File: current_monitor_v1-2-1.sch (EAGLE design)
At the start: 44 parts, among them IC1 LM4558D, SW1 RESET, SW2 Display, SW3 Display, U1 ATMEGA32U4-XUAU, Y1 16MHz

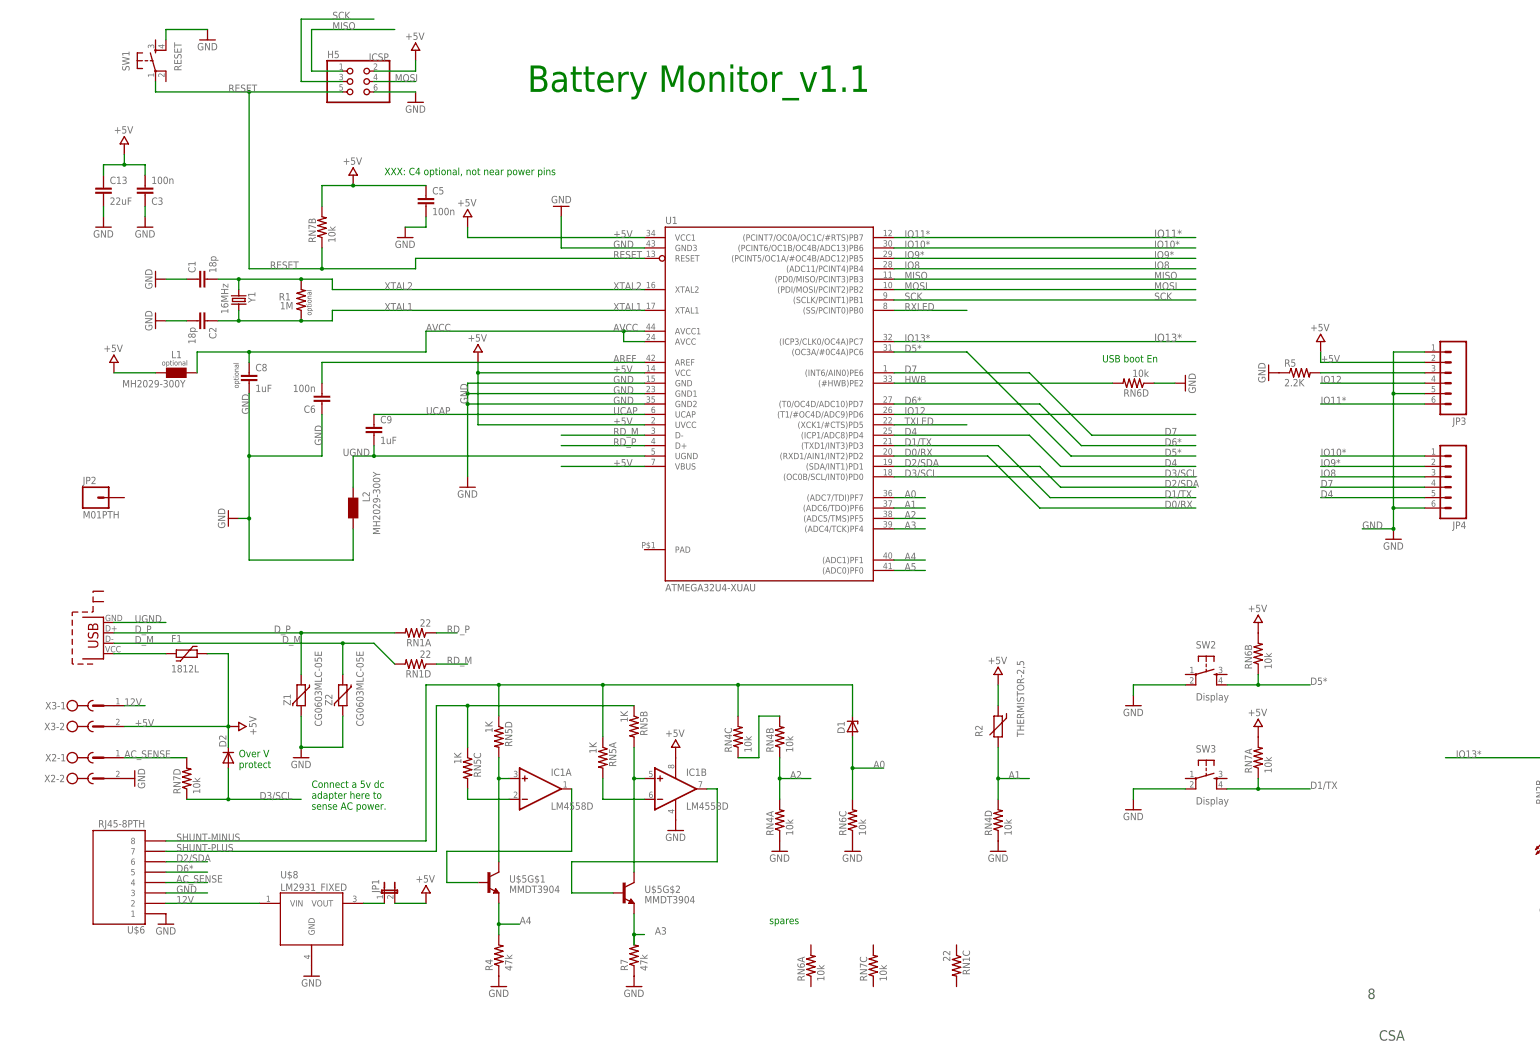
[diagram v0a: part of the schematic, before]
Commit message: submitted to fab 11/3/14 -- fixed agnd and usb drill sizes
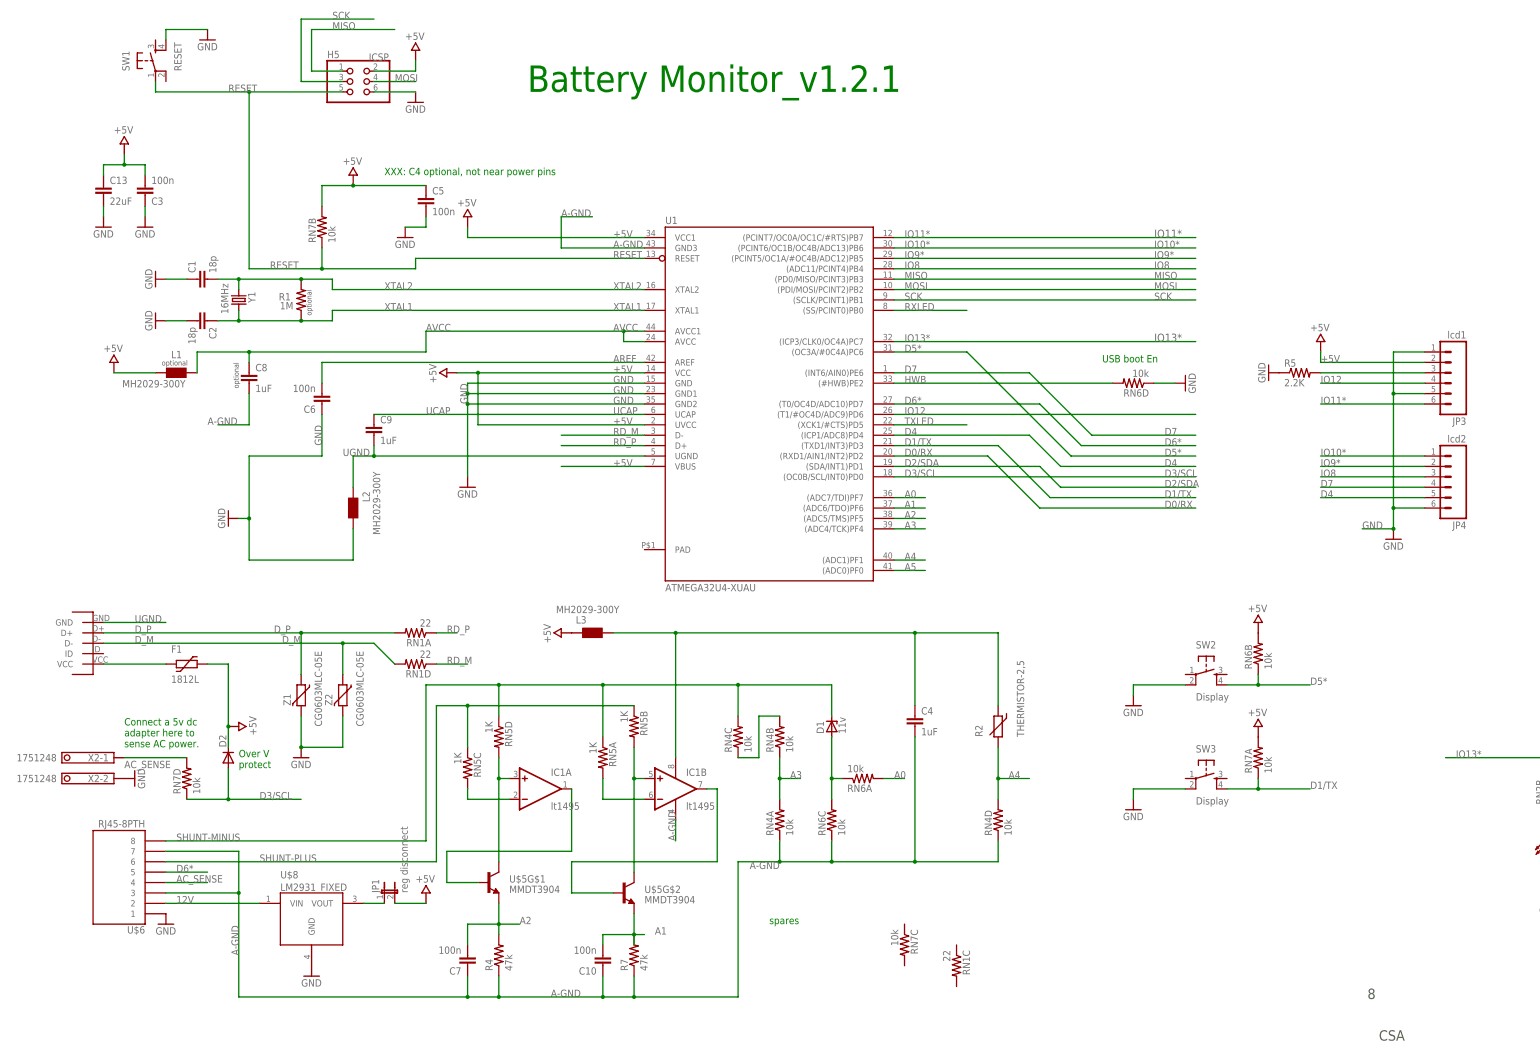
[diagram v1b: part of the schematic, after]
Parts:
- removed JP2: M01PTH, SparkFun-Connectors:M01PTH
- removed U$12: USB-MICRO-B-UNIVERSAL, _usb_micro_b:USB-MICRO-B-UNIVERSAL
- removed X3: (no value), con-phoenix-500:MSTBV2
- added C10, C7: 100n, SparkFun-Passives:CAP0805
- added C4: 1uF, SparkFun-Passives:CAP0805
- added L3: MH2029-300Y, wuerth-elektronik:WE-CBF_0805
- added U$16: USB-MICRO-B-DIGIKEY, gh_stuff:USB-MICRO-B-DIGIKEY
- D1: value (none) -> 11v
- IC1: value LM4558D -> lt1495
- JP1: value (none) -> reg disconnect
- JP3: value (none) -> lcd1
- JP4: value (none) -> lcd2
- X2: value (none) -> 1751248; device con-phoenix-500:MSTBV2 -> con-phoenix-350:1751248
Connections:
- new net A-GND: C10.1, C4.2, C7.1, C8.2, IC1P.V-, R4.1, R7.1, RN4A.1, RN4D.1, RN6C.1, U$6.3, U$6.7, U1.GND3
- new net N$13: D1.A, RN6A.1, RN6C.2
- new net N$15: C4.1, IC1P.V+, L3.2, R2.1
- net +5V: now also L3.1; no longer IC1P.V+, R2.1, X3-2.SK
- net 12V: no longer X3-1.SK
- net A0: now also RN6A.2; no longer D1.A, RN6C.2
- net A1: now also C10.2, R7.2, U$5G$2.E; no longer R2.2, RN4D.2
- net A2: now also C7.2, R4.2, U$5G$1.E; no longer RN4A.2, RN4B.1
- net A3: now also RN4A.2, RN4B.1; no longer R7.2, U$5G$2.E
- net A4: now also R2.2, RN4D.2; no longer R4.2, U$5G$1.E
- net AC_SENSE: now also X2-1.K; no longer X2-1.SK
- net D2/SDA: no longer U$6.6
- net D_M: now also U$16.D-; no longer U$12.D-
- net D_P: now also U$16.D+; no longer U$12.D+
- net GND: now also X2-2.K; no longer C8.2, IC1P.V-, R4.1, R7.1, RN4A.1, RN4D.1, RN6C.1, U$6.3, U1.GND3, X2-2.SK
- net N$7: now also U$16.VCC; no longer U$12.VBUS
- net SHUNT-PLUS: now also U$6.6; no longer U$6.7
- net UGND: now also U$16.GND; no longer U$12.GND
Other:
- note added: "Battery Monitor_v1.2.1"
- note removed: "Battery Monitor_v1.1"
- moved on the sheet: D1, F1, RN6A, RN6C, RN7C
